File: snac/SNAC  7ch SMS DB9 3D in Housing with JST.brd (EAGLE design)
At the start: 61.3 x 64.2 mm, 42 parts, among them IC1 4030D, Q1 BSS138, Q2 BSS138, Q3 BSS138, Q4 BSS138, Q5 BSS138, Q6 BSS138, Q7 BSS138, Q8 BSS138, Q9 BC849SMD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

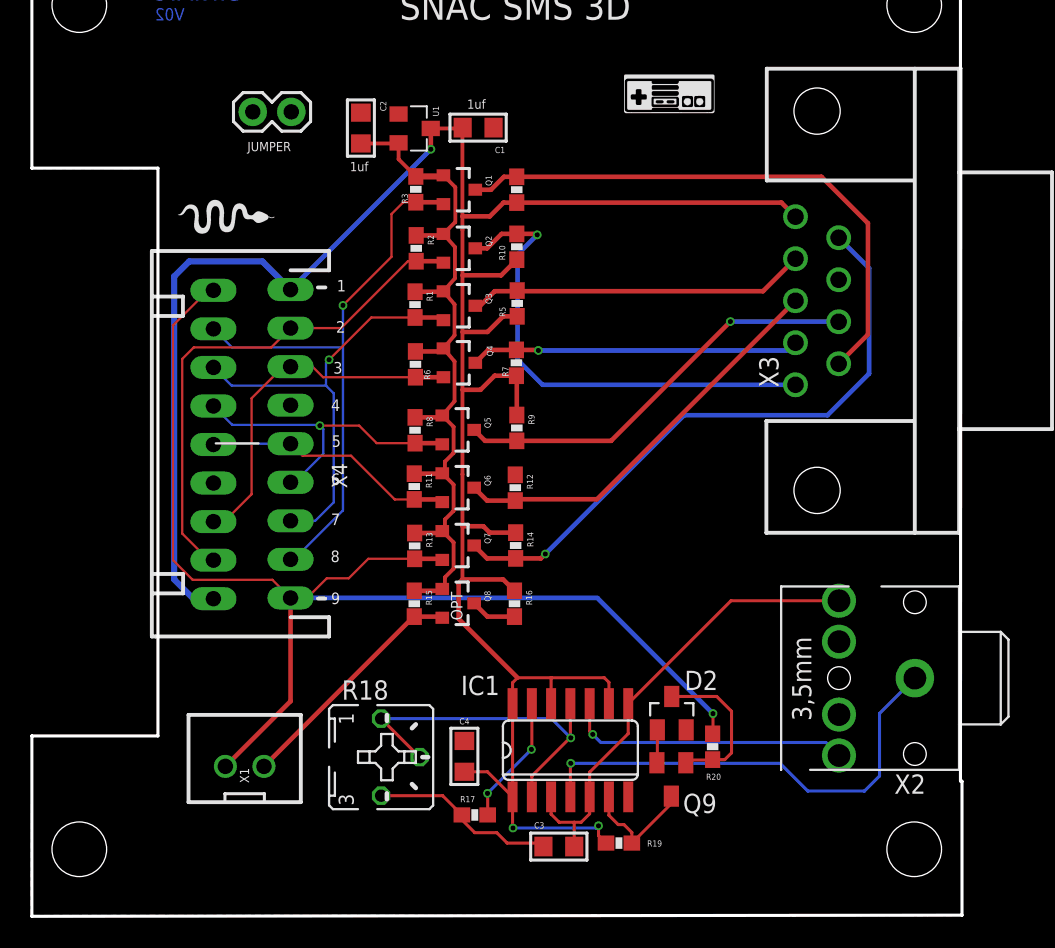
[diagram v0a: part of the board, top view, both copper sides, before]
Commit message: Updated SMS DB9 with JST version, and PCB image
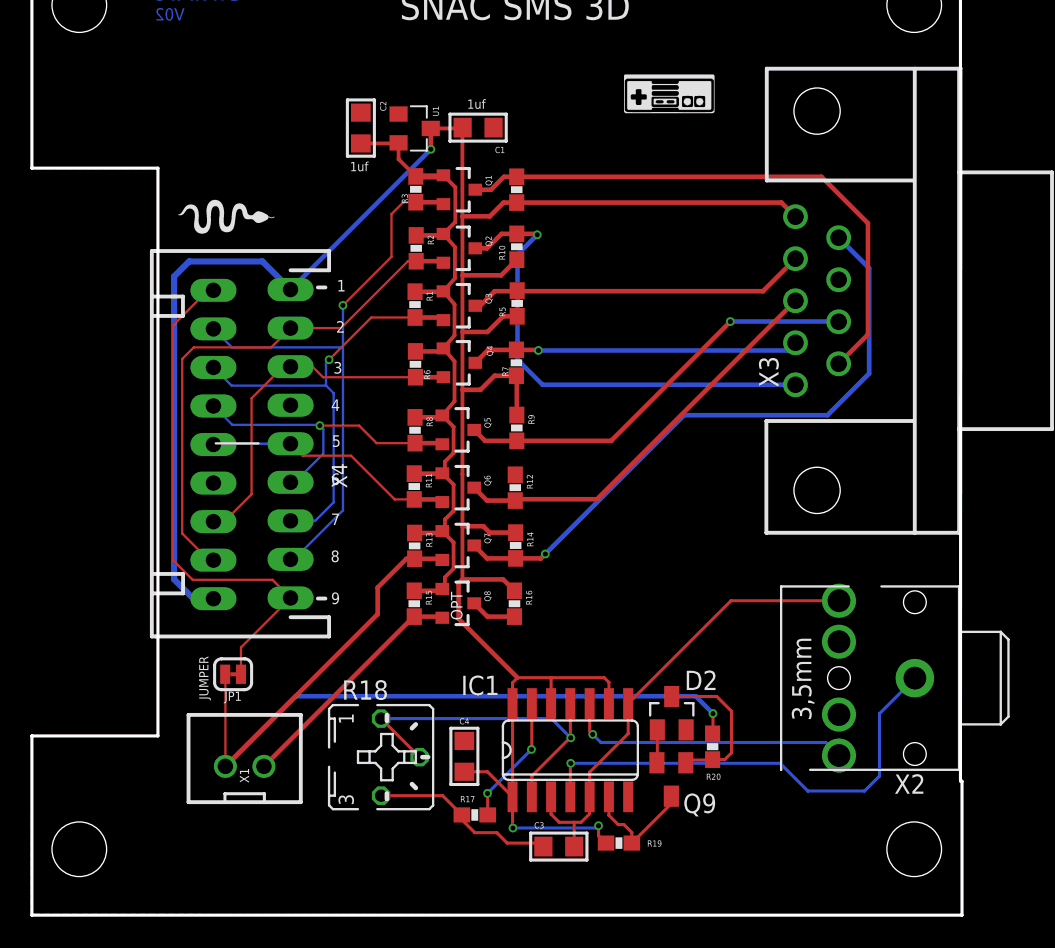
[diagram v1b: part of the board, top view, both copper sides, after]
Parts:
- removed JP3: (no value), SparkFun:1X02
- added JP1: JUMPER-SMT_2_NC_TRACE_SILK, SparkFun-Jumpers:SMT-JUMPER_2_NC_TRACE_SILK
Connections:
- net J1: now also JP1.1, X4.9, X5.9; no longer JP3.1
- net LV7: now also JP1.2; no longer JP3.2, X4.9, X5.9
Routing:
- net J1: track 0.00 -> 33.9 mm
- net LV7: track 84.2 -> 63.0 mm
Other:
- board size 61.3 x 64.2 mm -> 61.3 x 64.1 mm
- board text removed: "FOR USE WITH"
- board text removed: "GPIO7"
- board text removed: "MISTER"
- board text removed: "NEW IO BRD"
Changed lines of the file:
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@@
 <rectangle x1="30.642559375" y1="-26.370278125" x2="30.723840625" y2="-26.360121875" layer="21"/>
 <text x="6.2738" y="-29.8704" size="0.8128" layer="16" font="vector" ratio="22" rot="MR180">V02</text>
-<text x="16.1036" y="-34.4424" size="0.762" layer="22" font="vector" ratio="15" rot="MR0">MISTER</text>
 <text x="26.543" y="-70.2056" size="0.762" layer="21" font="vector" ratio="15" rot="R90">OPT</text>
-<text x="15.1384" y="-38.5064" size="0.6096" layer="22" font="vector" ratio="15" rot="MR0">GPIO7</text>
-<text x="16.5354" y="-41.0972" size="0.6096" layer="22" font="vector" ratio="15" rot="MR0">NEW IO BRD</text>
-<text x="17.0688" y="-40.2082" size="0.6096" layer="22" font="vector" ratio="15" rot="MR0">FOR USE WITH</text>
 <text x="26.8478" y="-36.4998" size="0.6096" layer="21" font="vector" ratio="15">1uf</text>
 <text x="19.1262" y="-40.6146" size="0.6096" layer="21" font="vector" ratio="15">1uf</text>
-<text x="15.6972" y="-35.6362" size="0.6096" layer="22" font="vector" ratio="15" rot="MR0">JUMPER</text>
-<text x="12.3698" y="-39.2938" size="0.6096" layer="21" font="vector" ratio="15">JUMPER</text>
+<text x="9.8044" y="-75.438" size="0.6096" layer="21" font="vector" ratio="15" rot="R90">JUMPER</text>
 <text x="22.4028" y="-30.6324" size="1.778" layer="21">SNAC SMS 3D</text>
 <wire x1="-1.8288" y1="-25.5016" x2="-1.8288" y2="-40.4114" width="0.2032" layer="20"/>
@@
 <wire x1="6.477" y1="-40.4114" x2="6.477" y2="-77.8256" width="0.2032" layer="20"/>
 <wire x1="6.477" y1="-77.8256" x2="-1.8288" y2="-77.8256" width="0.2032" layer="20"/>
-<wire x1="-1.8288" y1="-77.8256" x2="-1.8288" y2="-89.7128" width="0.2032" layer="20"/>
-<wire x1="-1.8288" y1="-89.7128" x2="59.4614" y2="-89.6366" width="0.2032" layer="20"/>
+<wire x1="-1.8288" y1="-77.8256" x2="-1.8288" y2="-89.6366" width="0.2032" layer="20"/>
+<wire x1="-1.8288" y1="-89.6366" x2="59.4614" y2="-89.6366" width="0.2032" layer="20"/>
 <wire x1="59.4614" y1="-89.6366" x2="59.4614" y2="-80.8228" width="0.2032" layer="20"/>
 <wire x1="59.4614" y1="-80.8228" x2="59.436" y2="-80.7974" width="0.2032" layer="20"/>
@@
 <attribute name="VALUE" x="20.21685" y="-35.88926875" size="0.889434375" layer="27" ratio="11" rot="R270"/>
 </element>
-<element name="JP3" library="SparkFun" package="1X02" value="" x="12.7254" y="-36.703" smashed="yes">
-<attribute name="VALUE" x="11.4554" y="-39.878" size="1.27" layer="27"/>
-</element>
 <element name="IC1" library="40xx" package="SO14" value="4030D" x="33.655" y="-78.7654" smashed="yes">
 <attribute name="NAME" x="26.4414" y="-75.1332" size="1.27" layer="25" ratio="10"/>
@@
 <element name="X4" library="Rembrandt Electronics - JST XH Connectors v1-0" package="JST-XH-09-PACKAGE-LONG-PAD" value="JST-XH-09-PIN-LONG-PAD" x="15.2146" y="-58.5724" rot="R90"/>
 <element name="X5" library="Rembrandt Electronics - JST XH Connectors v1-0" package="JST-XH-09-PACKAGE-LONG-PAD" value="JST-XH-09-PIN-LONG-PAD" x="10.1346" y="-58.6232" rot="MR270"/>
+<element name="JP1" library="SparkFun-Jumpers" package="SMT-JUMPER_2_NC_TRACE_SILK" package3d_urn="urn:adsk.eagle:package:39281/1" value="JUMPER-SMT_2_NC_TRACE_SILK" x="11.43" y="-73.7616" rot="R180"/>
 </elements>
 <signals>
@@
 <vertex x="59.436" y="-80.7974"/>
 <vertex x="59.436" y="-89.6112"/>
-<vertex x="-1.8796" y="-89.662"/>
+<vertex x="-1.8796" y="-89.5858"/>
 <vertex x="-1.8288" y="-77.8256"/>
 <vertex x="6.477" y="-77.8256"/>
@@
 <vertex x="59.436" y="-80.7974"/>
 <vertex x="59.436" y="-89.662"/>
-<vertex x="-1.8796" y="-89.662"/>
+<vertex x="-1.8796" y="-89.5858"/>
 <vertex x="-1.8288" y="-77.8256"/>
 <vertex x="6.477" y="-77.8256"/>
@@
 <wire x1="25.1382" y1="-66.1534" x2="23.3934" y2="-66.1534" width="0.3048" layer="1"/>
 <contactref element="X1" pad="1"/>
-<contactref element="JP3" pad="2"/>
 <contactref element="R20" pad="1"/>
 <via x="43.053" y="-76.3524" extent="1-16" drill="0.3302"/>
 <wire x1="43.0276" y1="-77.6868" x2="43.053" y2="-77.6614" width="0.2032" layer="1"/>
 <wire x1="43.053" y1="-77.6614" x2="43.053" y2="-76.3524" width="0.2032" layer="1"/>
-<contactref element="X4" pad="9"/>
-<contactref element="X5" pad="9"/>
-<wire x1="15.2146" y1="-68.7324" x2="14.0208" y2="-67.5386" width="0.1524" layer="1"/>
-<wire x1="14.0208" y1="-67.5386" x2="8.763" y2="-67.5386" width="0.1524" layer="1"/>
-<wire x1="8.763" y1="-67.5386" x2="7.4676" y2="-66.2432" width="0.1524" layer="1"/>
-<wire x1="9.779" y1="-48.4632" x2="10.1346" y2="-48.4632" width="0.1524" layer="1"/>
-<wire x1="7.4676" y1="-66.2432" x2="7.4676" y2="-50.7746" width="0.1524" layer="1"/>
-<wire x1="7.4676" y1="-50.7746" x2="9.779" y2="-48.4632" width="0.1524" layer="1"/>
-<wire x1="15.2146" y1="-68.7324" x2="16.3068" y2="-68.7324" width="0.1524" layer="1"/>
-<wire x1="17.6022" y1="-67.437" x2="19.05" y2="-67.437" width="0.1524" layer="1"/>
-<wire x1="16.3068" y1="-68.7324" x2="17.6022" y2="-67.437" width="0.1524" layer="1"/>
-<wire x1="20.3336" y1="-66.1534" x2="23.3934" y2="-66.1534" width="0.1524" layer="1"/>
-<wire x1="19.05" y1="-67.437" x2="20.3336" y2="-66.1534" width="0.1524" layer="1"/>
-<wire x1="15.2146" y1="-68.7324" x2="15.2146" y2="-75.5396" width="0.3048" layer="1"/>
-<wire x1="15.2146" y1="-75.5396" x2="10.922" y2="-79.8322" width="0.3048" layer="1"/>
-<wire x1="43.053" y1="-76.3524" x2="35.433" y2="-68.7324" width="0.3048" layer="16"/>
-<wire x1="35.433" y1="-68.7324" x2="15.2146" y2="-68.7324" width="0.3048" layer="16"/>
-<wire x1="15.2654" y1="-36.703" x2="10.1346" y2="-48.4632" width="0" layer="19" extent="1-1"/>
+<contactref element="JP1" pad="2"/>
+<wire x1="20.955" y1="-69.7992" x2="20.955" y2="-68.0466" width="0.3048" layer="1"/>
+<wire x1="20.955" y1="-68.0466" x2="22.8482" y2="-66.1534" width="0.3048" layer="1"/>
+<wire x1="22.8482" y1="-66.1534" x2="23.3934" y2="-66.1534" width="0.3048" layer="1"/>
+<wire x1="10.922" y1="-79.8322" x2="20.955" y2="-69.7992" width="0.3048" layer="1"/>
+<wire x1="10.922" y1="-79.8322" x2="10.922" y2="-73.7743" width="0.1524" layer="1"/>
+<wire x1="10.922" y1="-73.7743" x2="10.9093" y2="-73.7616" width="0.1524" layer="1"/>
+<wire x1="43.053" y1="-76.3524" x2="41.91" y2="-75.2094" width="0.3048" layer="16"/>
+<wire x1="15.5448" y1="-75.2094" x2="10.922" y2="-79.8322" width="0.3048" layer="16"/>
+<wire x1="41.91" y1="-75.2094" x2="15.5448" y2="-75.2094" width="0.3048" layer="16"/>
 </signal>
 <signal name="HV7">
@@
 </signal>
 <signal name="N$4">
-</signal>
-<signal name="J1">
-<contactref element="JP3" pad="1"/>
 </signal>
 <signal name="N$5">
@@
 <signal name="N$22">
 </signal>
+<signal name="J1">
+<contactref element="X5" pad="9"/>
+<contactref element="JP1" pad="1"/>
+<contactref element="X4" pad="9"/>
+<wire x1="15.2146" y1="-68.7324" x2="14.0208" y2="-67.5386" width="0.1524" layer="1"/>
+<wire x1="14.0208" y1="-67.5386" x2="8.763" y2="-67.5386" width="0.1524" layer="1"/>
+<wire x1="8.763" y1="-67.5386" x2="7.4676" y2="-66.2432" width="0.1524" layer="1"/>
+<wire x1="7.4676" y1="-66.2432" x2="7.4676" y2="-50.7746" width="0.1524" layer="1"/>
+<wire x1="7.4676" y1="-50.7746" x2="9.779" y2="-48.4632" width="0.1524" layer="1"/>
+<wire x1="15.2146" y1="-68.7324" x2="11.9507" y2="-71.9963" width="0.1524" layer="1"/>
+<wire x1="11.9507" y1="-71.9963" x2="11.9507" y2="-73.7616" width="0.1524" layer="1"/>
+<wire x1="9.779" y1="-48.4632" x2="10.1346" y2="-48.4632" width="0" layer="19" extent="1-1"/>
+</signal>
 </signals>

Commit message: changed from LV7 to LV5 pin on the DB9 3D with JST design
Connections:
- net LV5: now also R20.1
- net LV7: no longer R20.1
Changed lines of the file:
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@@
 <wire x1="20.8906" y1="-58.5334" x2="23.4188" y2="-58.5334" width="0.1524" layer="1"/>
 <wire x1="19.7358" y1="-57.3786" x2="20.8906" y2="-58.5334" width="0.1524" layer="1"/>
+<contactref element="R20" pad="1"/>
+<wire x1="43.0276" y1="-77.6868" x2="25.2128" y2="-58.608" width="0" layer="19" extent="1-1"/>
 </signal>
 <signal name="HV5">
@@
 <wire x1="25.1382" y1="-66.1534" x2="23.3934" y2="-66.1534" width="0.3048" layer="1"/>
 <contactref element="X1" pad="1"/>
-<contactref element="R20" pad="1"/>
 <via x="43.053" y="-76.3524" extent="1-16" drill="0.3302"/>
-<wire x1="43.0276" y1="-77.6868" x2="43.053" y2="-77.6614" width="0.2032" layer="1"/>
 <wire x1="43.053" y1="-77.6614" x2="43.053" y2="-76.3524" width="0.2032" layer="1"/>
 <contactref element="JP1" pad="2"/>

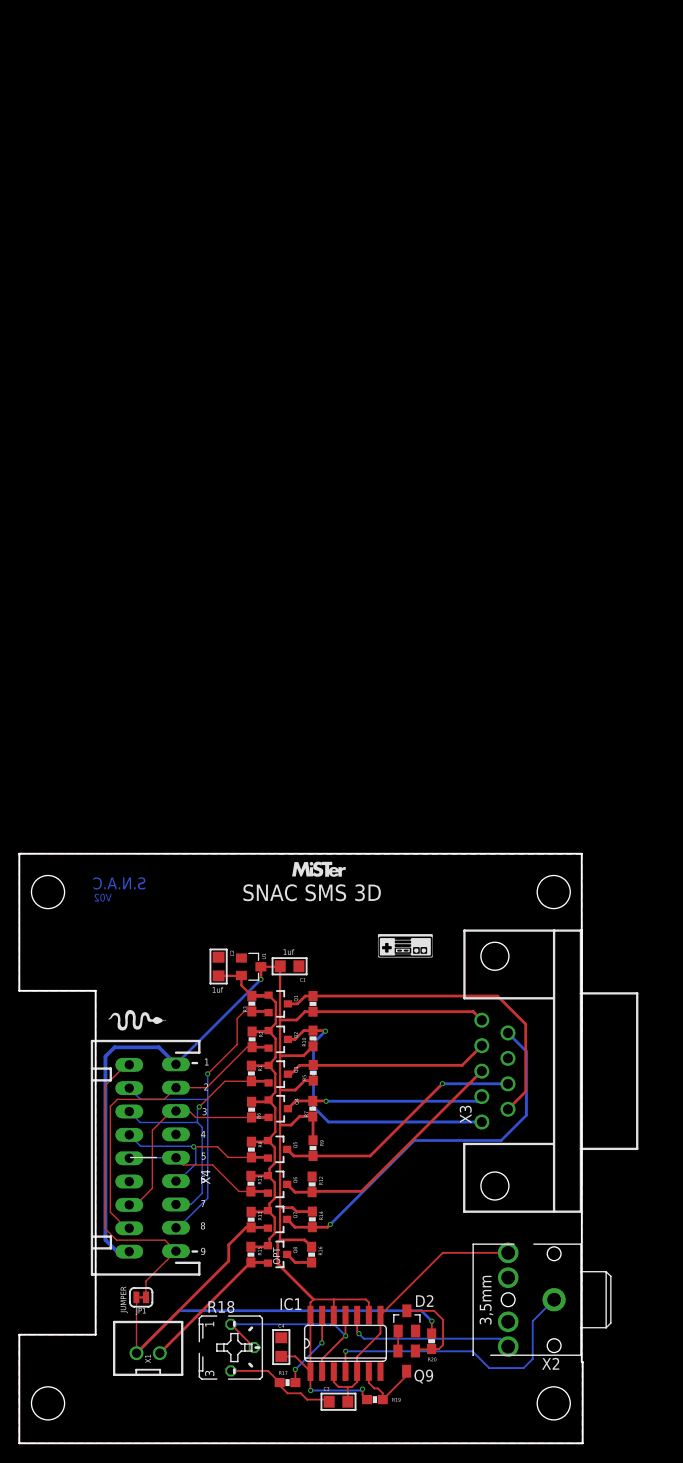
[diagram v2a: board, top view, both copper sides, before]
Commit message: Added charge pump to the SMS 3D and SMS DB9 3D PCBs
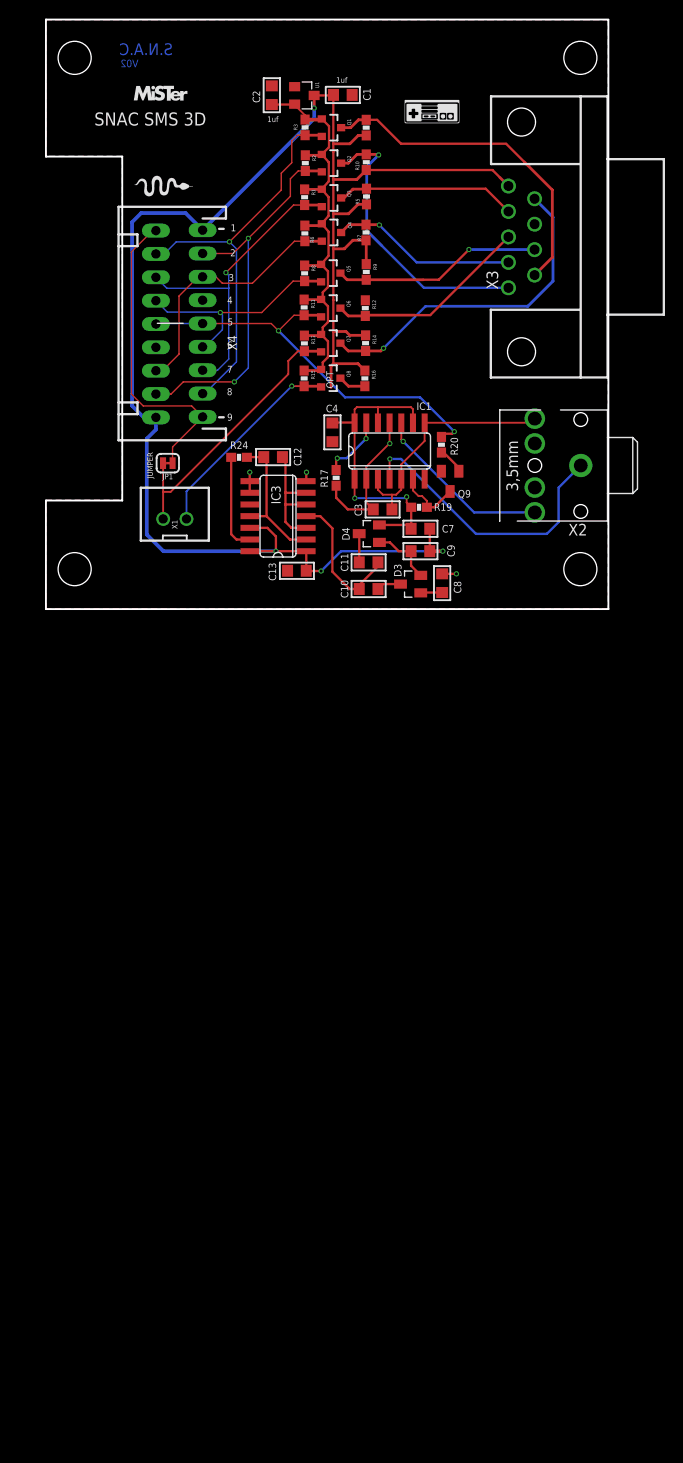
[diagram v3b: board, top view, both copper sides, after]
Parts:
- removed D2: BAT54, diode:SOT23
- removed R18: 47K, pot:B25P
- added C10, C11, C7, C8, C9: 2.2uF, rc-master-smd:C0805
- added C12: 10nF, rc-master-smd:C0805
- added C13: 22uF, rc-master-smd:C0805
- added D3, D4: BAS40-04, diode:SOT23
- added IC3: 4030D, 40xx:SO14
- added R24: 75K, SparkFun:0603-RES
- R17: value 22K -> 75K
- moved C4 99.7 mm to (32.2, 20.3), turned to 270 degrees
- moved R17 98.6 mm to (32.6, 15.4), turned to 270 degrees
- moved R20 97.5 mm to (44.1, 19.0)
- moved C3 97.2 mm to (37.7, 12.0)
- moved IC1 97.2 mm to (38.5, 18.3)
- moved R19 97.2 mm to (41.7, 12.2)
- moved Q9 95.8 mm to (45.0, 15.0)
- moved Q1 95.5 mm to (32.1, 53.5)
- moved Q2 95.5 mm to (32.1, 49.6)
- moved Q3 95.5 mm to (32.1, 45.8)
- moved Q4 95.5 mm to (32.1, 42.1)
- moved Q5 95.5 mm to (32.0, 37.7)
- moved Q6 95.5 mm to (32.0, 33.9)
- moved Q7 95.5 mm to (32.0, 30.0)
- moved Q8 95.5 mm to (32.0, 26.2)
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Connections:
- removed net N$10: IC1.13, R17.2
- new net 10V: C4.1, C7.1, D4.2, IC1.1, IC1.12, IC1.14, IC1.9, R19.1
- new net N$27: C9.1, D3.2, D4.1
- new net N$28: C8.1, D3.1
- new net N$29: C11.2, D4.3
- new net N$30: C10.2, D3.3
- new net N$31: C12.1, IC3.11, IC3.2, R24.2
- new net N$32: IC3.13, R24.1
- new net N$33: C10.1, C11.1, IC3.4
- new net N$34: C12.2, IC3.3, IC3.5, IC3.6
- net GND: now also C13.2, C8.2, IC3.7, IC3.8, IC3.9; no longer D2.1
- net HV: now also C13.1, C7.2, C9.2, IC3.1, IC3.12, IC3.14; no longer C4.1, IC1.1, IC1.12, IC1.14, IC1.9, R19.1
- net LV5: no longer R20.1
- net LV6: now also R20.1
- net N$14: no longer D2.3
- net N$5: now also C3.1, R17.2; no longer R18.A, R18.S
- net N$9: now also IC1.13; no longer C3.1, R18.E
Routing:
- net 10V: track 0.00 -> 34.9 mm, vias 0 -> 2
- net LV7: track 62.9 -> 30.5 mm, vias 1 -> 0
- net LV6: track 16.7 -> 44.4 mm, vias 0 -> 2
- net HV: track 161.5 -> 188.6 mm, vias 3 -> 4
- net N$31: track 0.00 -> 15.6 mm
- net N$33: track 0.00 -> 15.6 mm
- net N$34: track 0.00 -> 14.3 mm
- net N$32: track 0.00 -> 10.9 mm
- net LV2: track 34.2 -> 43.2 mm, vias 0 -> 2
- net N$10: track 8.56 -> 0.00 mm, vias 2 -> 0
- net N$14: track 10.4 -> 2.96 mm
- net N$5: track 23.9 -> 16.7 mm
- net N$27: track 0.00 -> 6.91 mm
- net LV8: track 16.0 -> 22.6 mm, vias 0 -> 1
- net LV1: track 38.5 -> 44.4 mm
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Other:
- board size 61.3 x 64.1 mm -> 61.2 x 64.1 mm
- board text removed: "+"
- board text removed: "-"
